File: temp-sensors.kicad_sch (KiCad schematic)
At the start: 33 parts, among them U34 TMP75AIDR, U35 TMP75AIDR, U36 TMP75AIDR

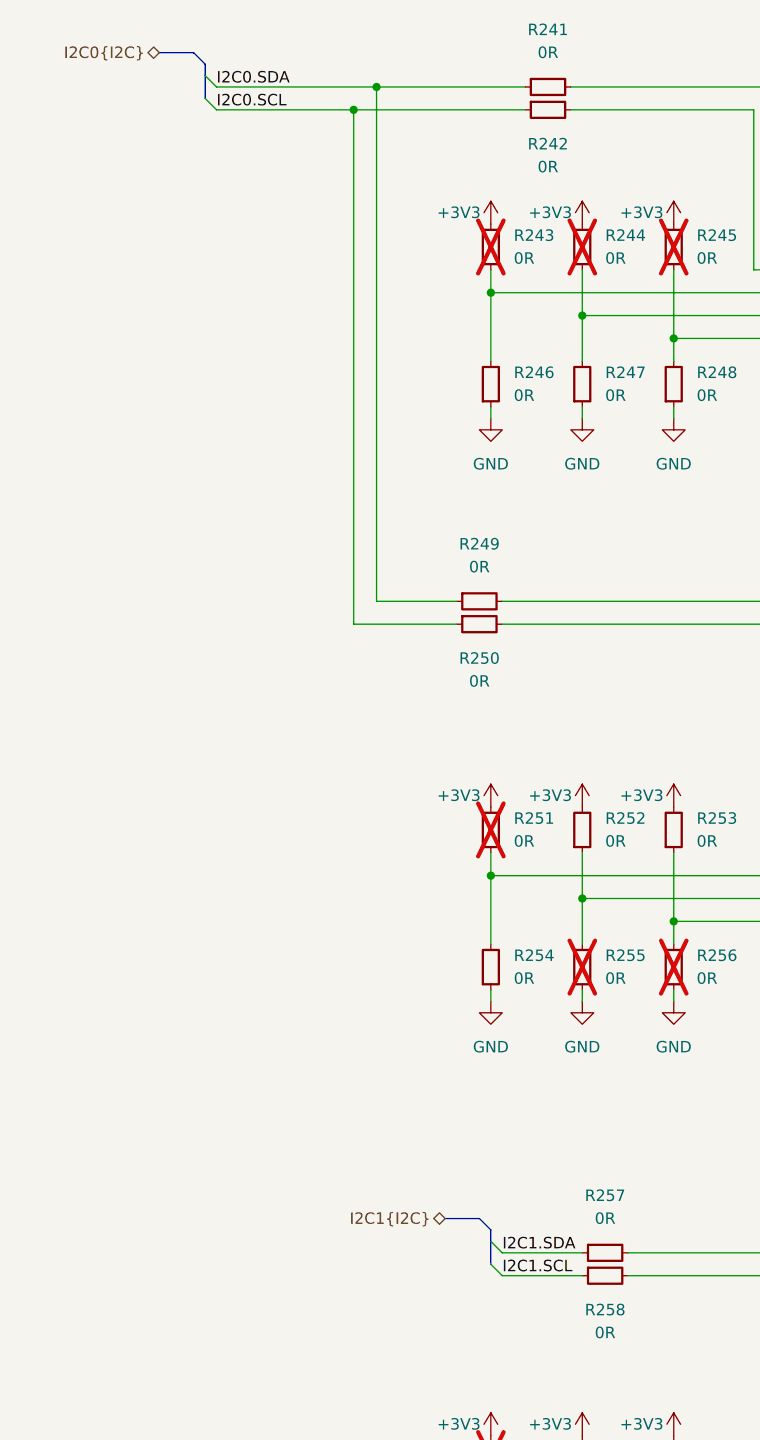
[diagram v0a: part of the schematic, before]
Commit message: [#83362] Fix connections of headers, add I2C mux
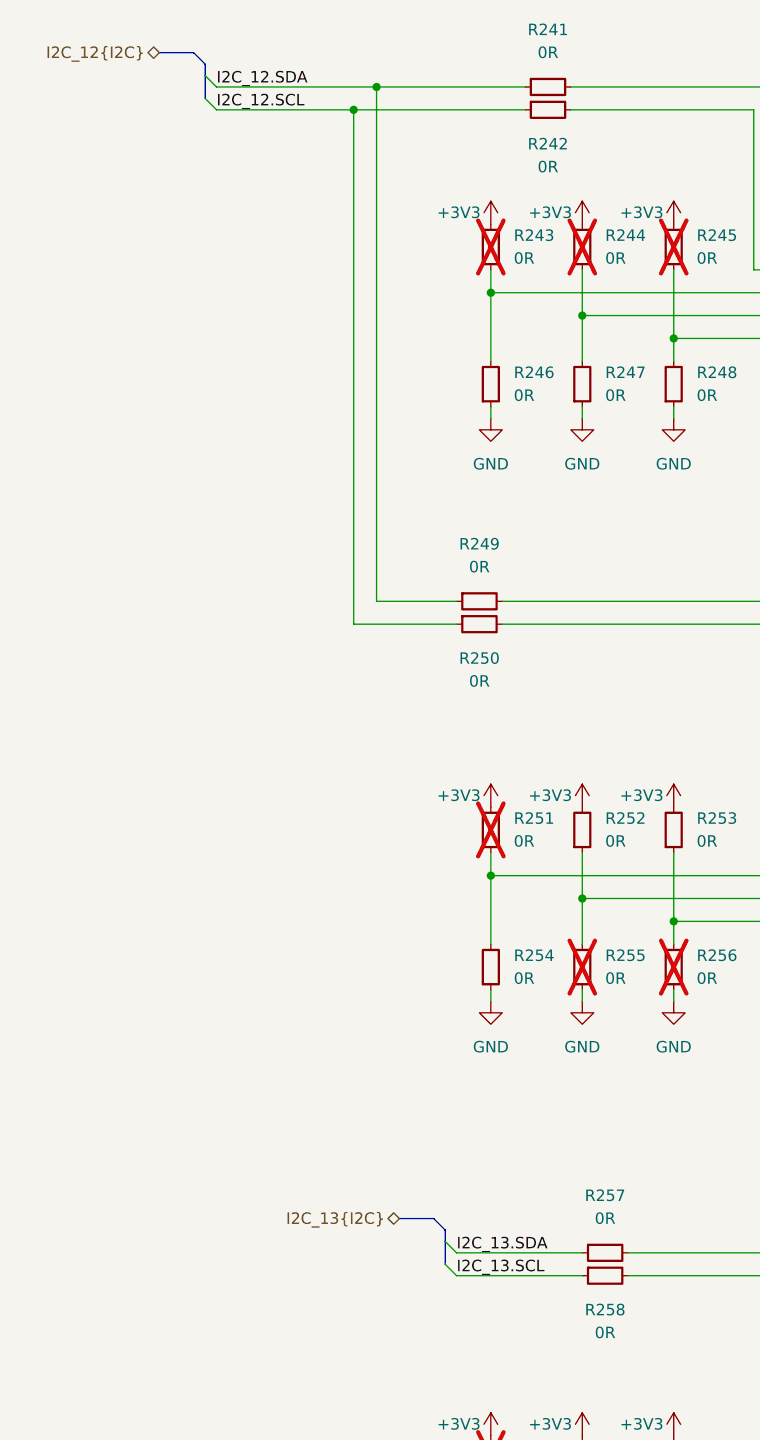
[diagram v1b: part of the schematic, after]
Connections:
- net I2C0.SCL renamed I2C_12.SCL
- net I2C0.SDA renamed I2C_12.SDA
- net I2C1.SCL renamed I2C_13.SCL
- net I2C1.SDA renamed I2C_13.SDA
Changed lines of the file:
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@@
 	)
 	(bus_entry
-		(at 184.15 196.85)
+		(at 179.07 196.85)
 		(size 1.27 1.27)
 		(stroke
@@
 	)
 	(bus_entry
-		(at 184.15 199.39)
+		(at 179.07 199.39)
 		(size 1.27 1.27)
 		(stroke
@@
 	(bus
 		(pts
-			(xy 184.15 196.85) (xy 184.15 199.39)
+			(xy 179.07 196.85) (xy 179.07 199.39)
 		)
 		(stroke
@@
 	(bus
 		(pts
-			(xy 179.07 194.31) (xy 182.88 194.31)
+			(xy 173.99 194.31) (xy 177.8 194.31)
 		)
 		(stroke
@@
 	(bus
 		(pts
-			(xy 184.15 195.58) (xy 184.15 196.85)
+			(xy 179.07 195.58) (xy 179.07 196.85)
 		)
 		(stroke
@@
 	(bus
 		(pts
-			(xy 182.88 194.31) (xy 184.15 195.58)
+			(xy 177.8 194.31) (xy 179.07 195.58)
 		)
 		(stroke
@@
 	(wire
 		(pts
-			(xy 185.42 198.12) (xy 194.31 198.12)
+			(xy 180.34 198.12) (xy 194.31 198.12)
 		)
 		(stroke
@@
 	(wire
 		(pts
-			(xy 185.42 200.66) (xy 194.31 200.66)
+			(xy 180.34 200.66) (xy 194.31 200.66)
 		)
 		(stroke
@@
 		)
 	)
-	(label "I2C0.SCL"
+	(label "I2C_12.SCL"
 		(at 153.67 71.12 0)
 		(effects
@@
 		)
 	)
-	(label "I2C1.SDA"
-		(at 185.42 198.12 0)
+	(label "I2C_13.SDA"
+		(at 180.34 198.12 0)
 		(effects
 			(font
@@
 		)
 	)
-	(label "I2C0.SDA"
+	(label "I2C_12.SDA"
 		(at 153.67 68.58 0)
 		(effects
@@
 		)
 	)
-	(label "I2C1.SCL"
-		(at 185.42 200.66 0)
+	(label "I2C_13.SCL"
+		(at 180.34 200.66 0)
 		(effects
 			(font
@@
 		)
 	)
-	(hierarchical_label "I2C1{I2C}"
+	(hierarchical_label "I2C_13{I2C}"
 		(shape bidirectional)
-		(at 179.07 194.31 180)
+		(at 173.99 194.31 180)
 		(effects
 			(font
@@
 		)
 	)
-	(hierarchical_label "I2C0{I2C}"
+	(hierarchical_label "I2C_12{I2C}"
 		(shape bidirectional)
 		(at 147.32 64.77 180)

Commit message: [#83609] Reannotate board
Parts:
- renumbered C26 to C172, C63 to C173, C155 to C174, R249 to R293, R250 to R294, R243 to R295, R246 to R296, R251 to R297, R254 to R298, R259 to R299, R262 to R300, R241 to R301, R242 to R302, R244 to R303, R247 to R304, R252 to R305, R255 to R306, R257 to R307, R258 to R308, R260 to R309, R263 to R310, R245 to R311, R248 to R312, R253 to R313, R256 to R314, R261 to R315, R264 to R316, TP65 to TP25, TP66 to TP26, TP67 to TP27, U34 to U38, U35 to U39, U36 to U40

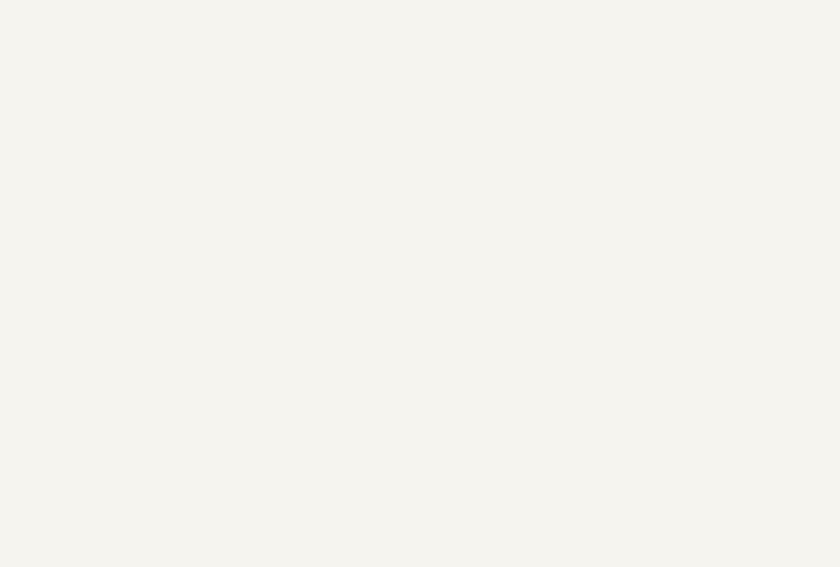
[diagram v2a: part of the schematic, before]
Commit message: [#83904] Connect OSM_I2C_A bus to temperature sensors via 0Rs
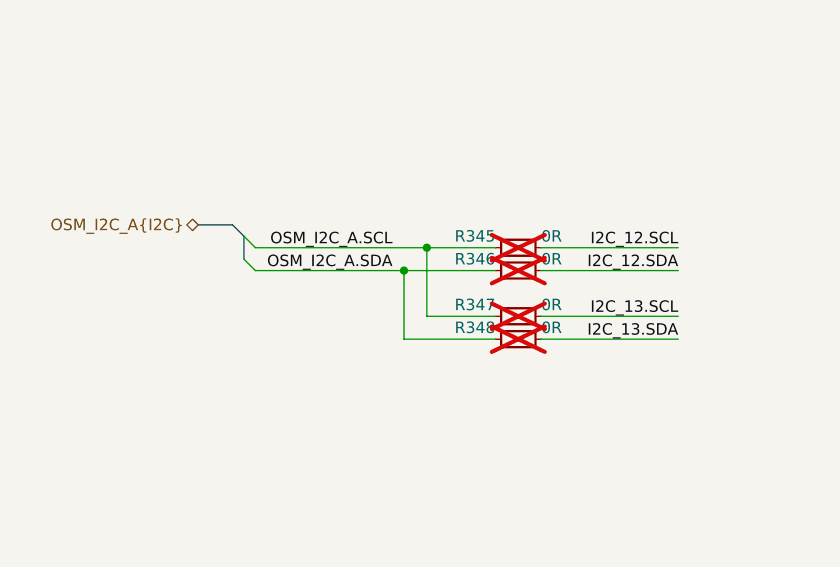
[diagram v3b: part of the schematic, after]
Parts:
- added R345, R346, R347, R348: R_0R_0402, antmicro-footprints:R_0402_1005Metric, symbol antmicroResistors0402:R_0R_0402
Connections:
- net I2C_12.SCL: now also R345.2
- net I2C_12.SDA: now also R346.2
- net I2C_13.SCL: now also R347.2
- net I2C_13.SDA: now also R348.2
- new net OSM_I2C_A.SCL: R345.1, R347.1
- new net OSM_I2C_A.SDA: R346.1, R348.1

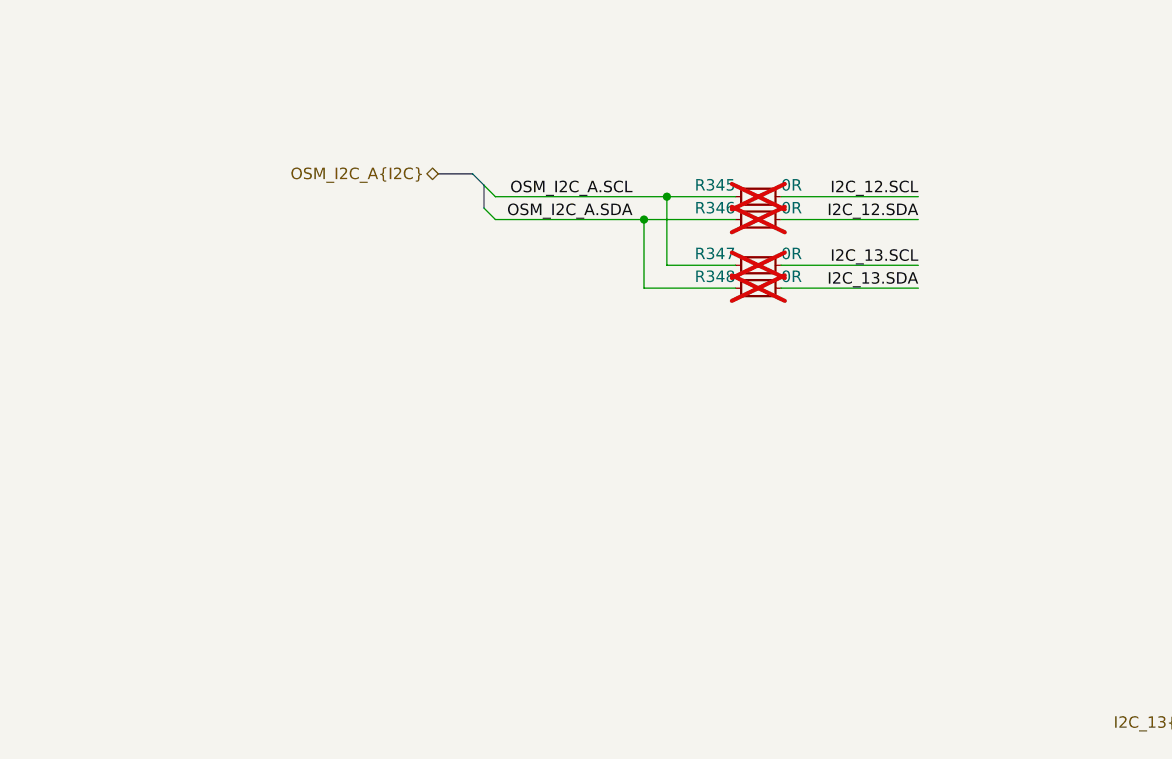
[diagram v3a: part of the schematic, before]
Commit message: [#83904] Add level shifters, clear ERC
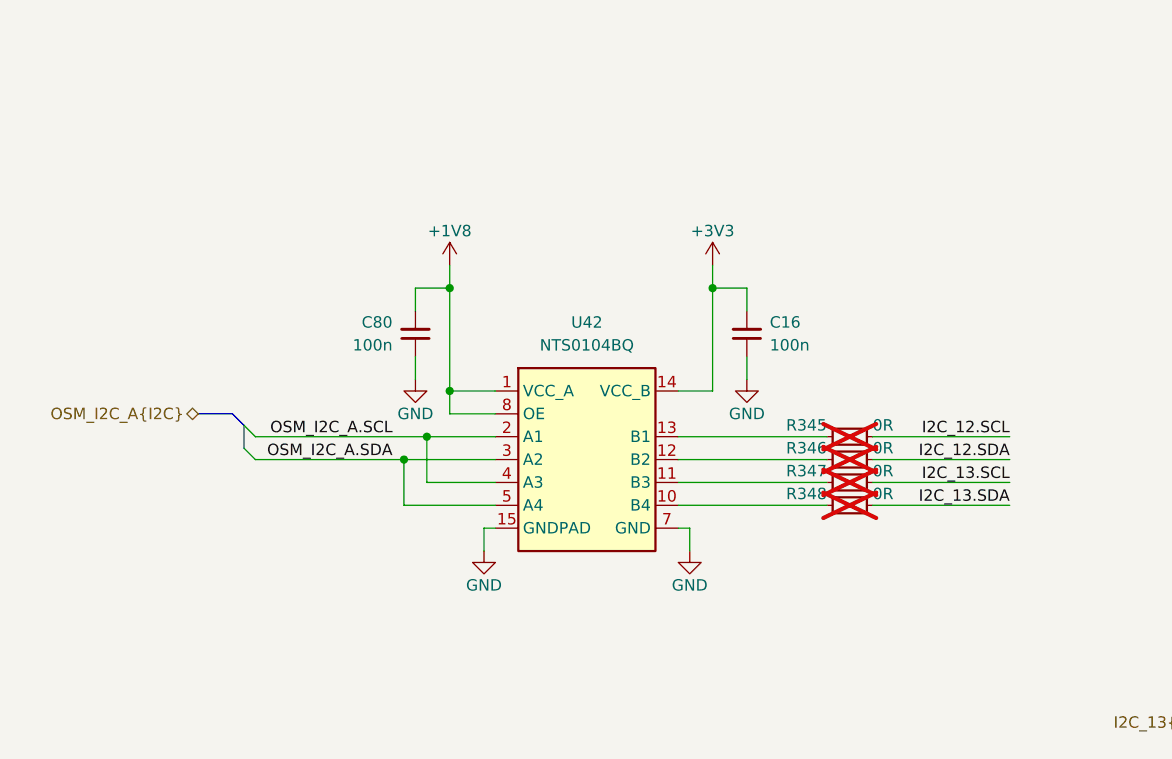
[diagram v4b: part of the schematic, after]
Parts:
- added C16, C80: C_100n_0402, antmicro-footprints:C_0402_1005Metric, symbol antmicroCapacitors0402:C_100n_0402
- added U42: NTS0104_DHVQFN, antmicro-footprints:DHVQFN-14-1EP_2.5x3mm, symbol antmicroLogicTranslatorsLevelShifters:NTS0104_DHVQFN
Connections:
- net +3V3: now also C16.2, U42.14 (VCC_B)
- net GND: now also C16.1, C80.1, U42.15 (GNDPAD), U42.7 (GND)
- net OSM_I2C_A.SCL: now also U42.2 (A1), U42.4 (A3); no longer R345.1, R347.1
- net OSM_I2C_A.SDA: now also U42.3 (A2), U42.5 (A4); no longer R346.1, R348.1
- new net: R347.1, U42.11 (B3)
- new net: R348.1, U42.10 (B4)
- new net: R346.1, U42.12 (B2)
- new net: R345.1, U42.13 (B1)
- new net +1V8: C80.2, U42.1 (VCC_A), U42.8 (OE)
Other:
- moved on the sheet: R345, R346, R347, R348
